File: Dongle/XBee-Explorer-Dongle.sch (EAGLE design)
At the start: 26 parts, among them U1 FT232RL-BASICSSOP, U2 XBEE-1B3, U3 V_REG_LDOSMD

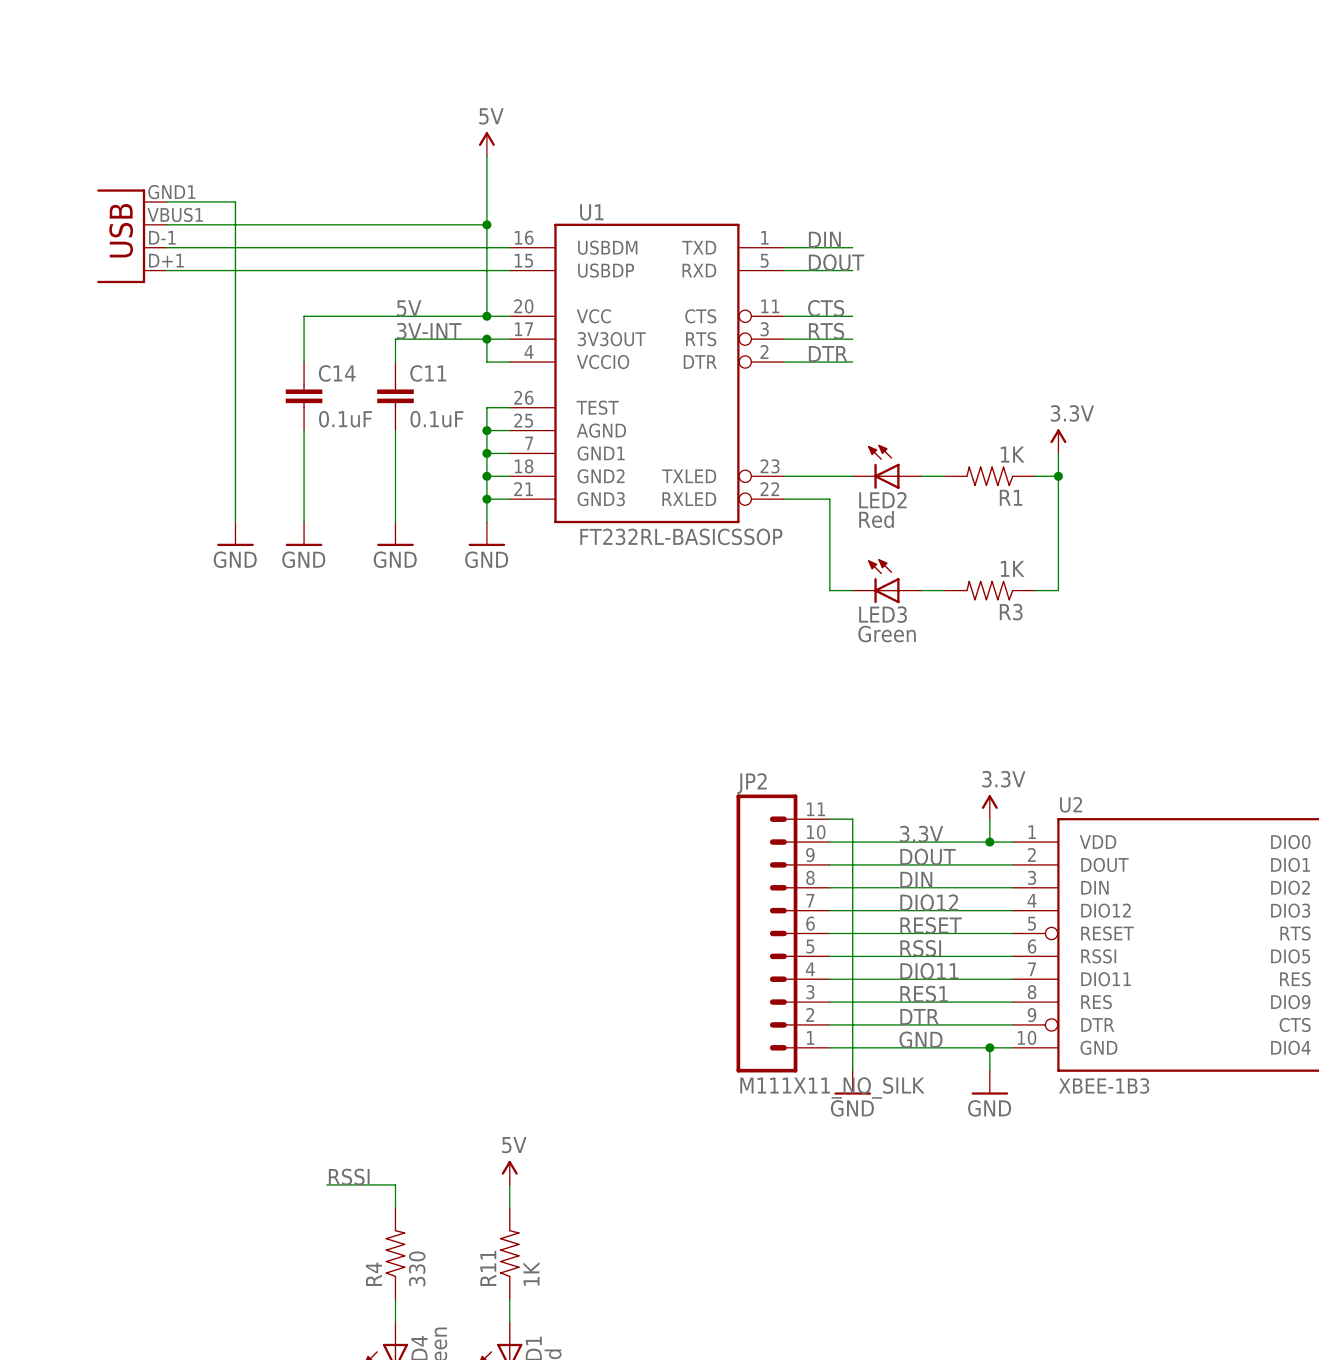
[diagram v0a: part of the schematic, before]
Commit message: XBee Dongle transition to FT231X
FT231X replaces the FT232RL.
Additional components added (R2, R5, C3, C4).
Updated all resistor and capacitor packages to 0603 footprints.
Rearranged Vreg circuit layout.
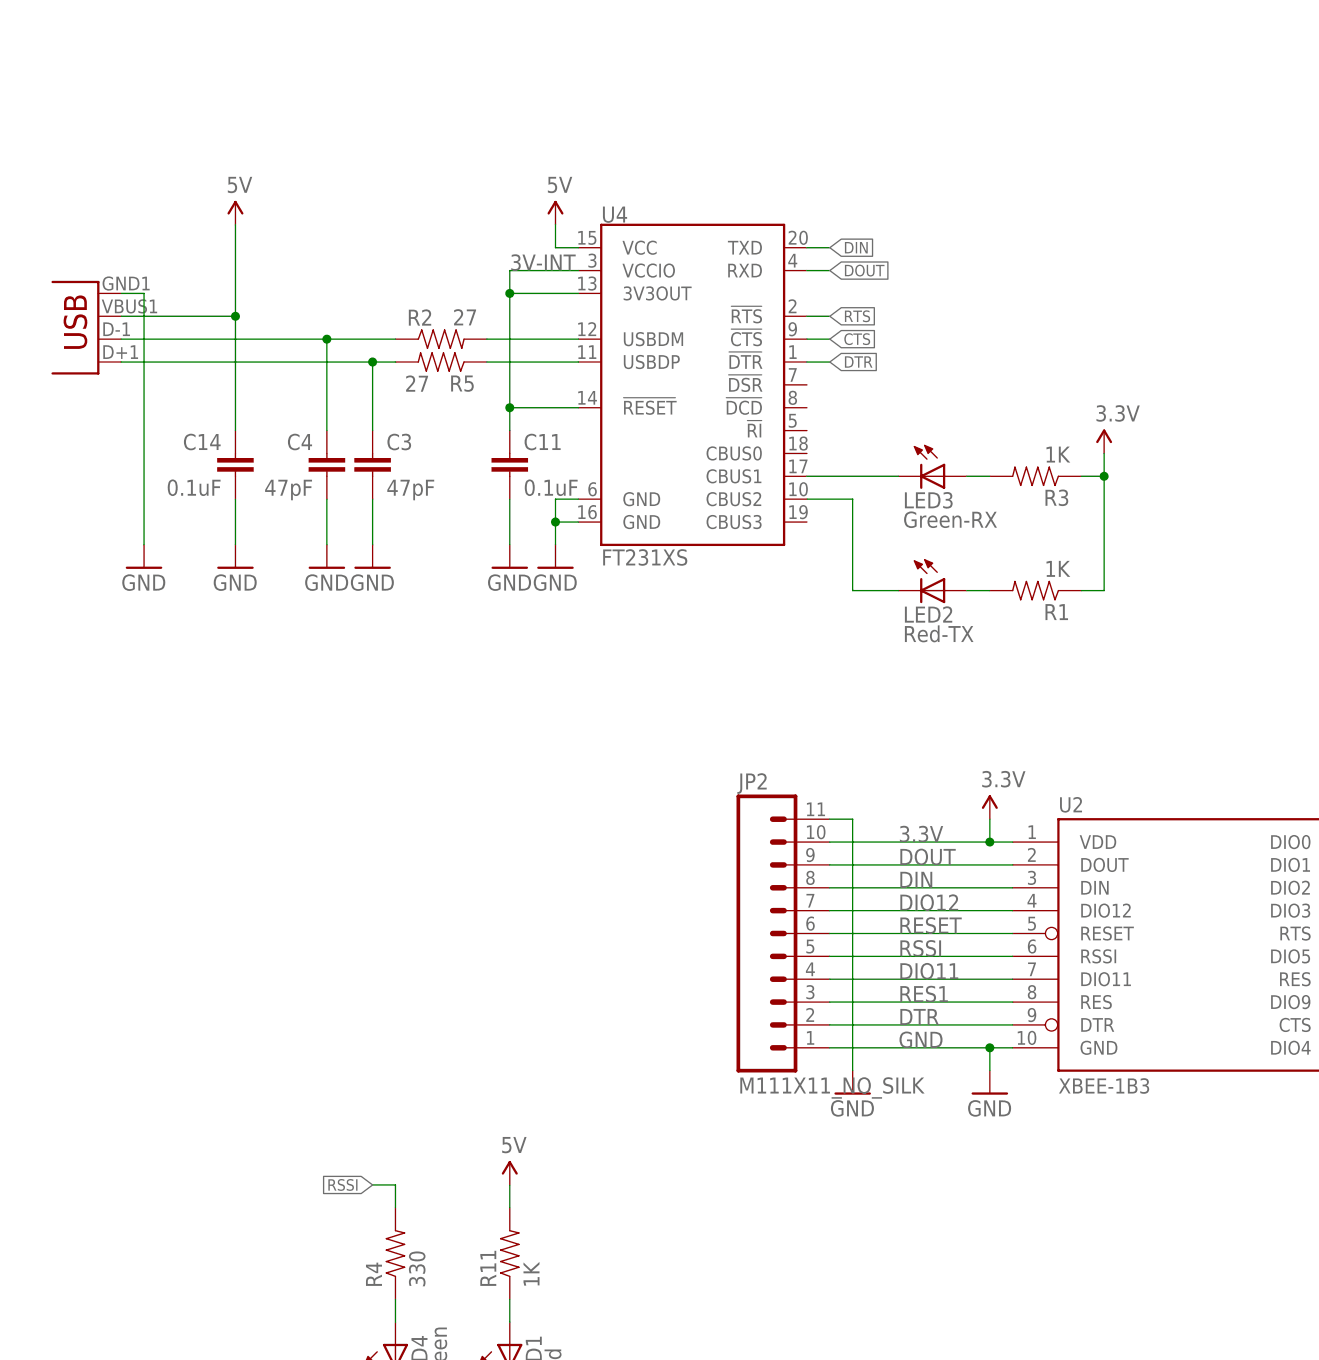
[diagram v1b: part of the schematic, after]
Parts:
- removed U1: FT232RL-BASICSSOP, SparkFun:FT232RL-BASICSSOP
- added C3, C4: 47pF, SparkFun:CAP0603-CAP
- added R2, R5: 27, SparkFun:RESISTOR0603-RES
- added U4: FT231XS, SparkFun-DigitalIC:FT231XS
- C11, C14, C2: device SparkFun:CAP0402-CAP -> SparkFun:CAP0603-CAP
- LED2: value Red -> Red-TX
- LED3: value Green -> Green-RX
- R1, R11, R3, R4: device SparkFun:RESISTOR0402-RES -> SparkFun:RESISTOR0603-RES
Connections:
- new net N$5: R2.2, U4.USBDM
- new net N$6: C3.1, JP1.D+, R5.2
- net 3V-INT: now also U4.!RESET, U4.3V3OUT, U4.VCCIO; no longer U1.3V3OUT, U1.VCCIO
- net 5V: now also U4.VCC; no longer U1.VCC
- net CTS: now also U4.!CTS; no longer U1.CTS
- net DIN: now also U4.TXD; no longer U1.TXD
- net DOUT: now also U4.RXD; no longer U1.RXD
- net DTR: now also U4.!DTR; no longer U1.DTR
- net GND: now also C3.2, C4.2, U4.GND@16, U4.GND@6; no longer U1.AGND, U1.GND1, U1.GND2, U1.GND3, U1.TEST
- net N$3: now also C4.1, R2.1; no longer U1.USBDM
- net N$7: now also R5.1, U4.USBDP; no longer JP1.D+, U1.USBDP
- net RTS: now also U4.!RTS; no longer U1.RTS
- net RXLED: now also U4.CBUS1; no longer U1.RXLED
- net TXLED: now also U4.CBUS2; no longer U1.TXLED
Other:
- moved on the sheet: C11, C14, LED2, LED3, R1, R3

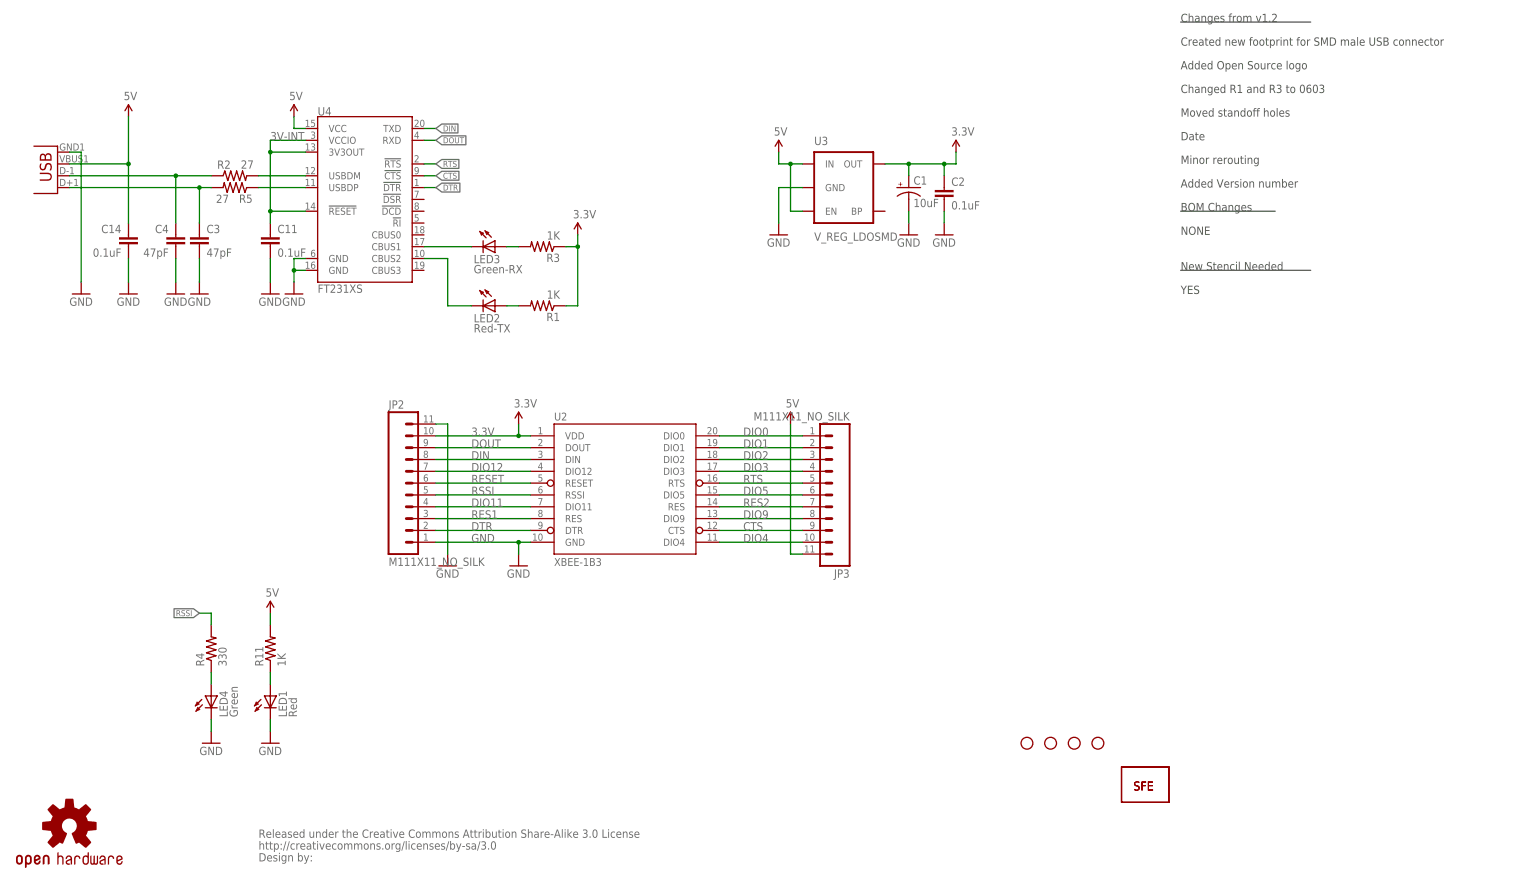
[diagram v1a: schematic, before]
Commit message: Added jumper to disconnect RSSI LED, moved silk
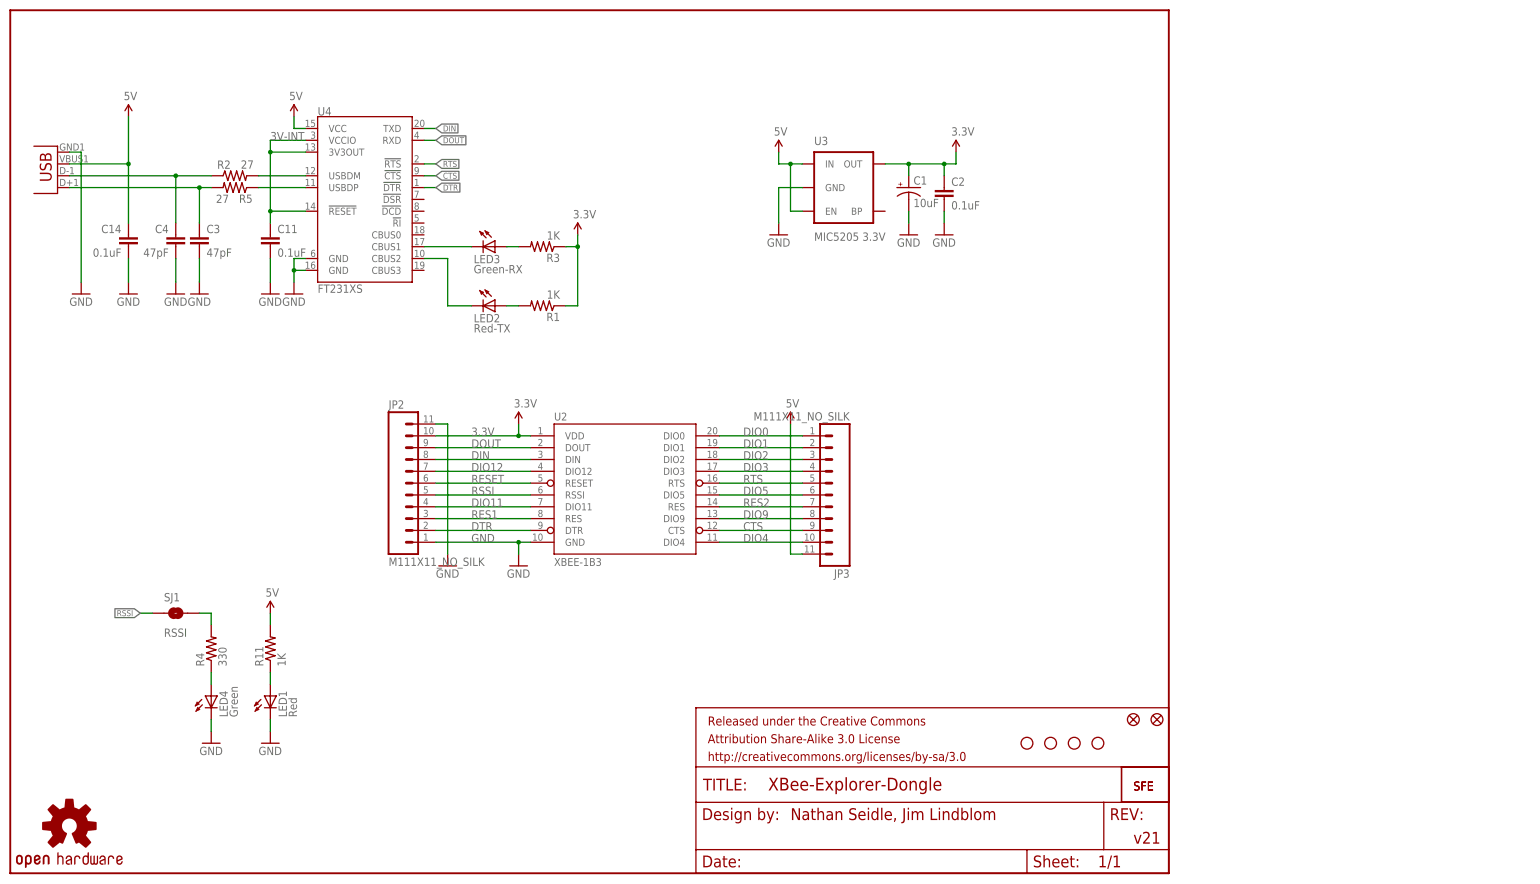
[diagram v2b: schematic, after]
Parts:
- removed U$8: OSHW-LOGOS, SparkFun:OSHW-LOGOS
- added FID1, FID2: FIDUCIALUFIDUCIAL, SparkFun-Aesthetics:FIDUCIALUFIDUCIAL
- added FRAME1: FRAME-LETTER, SparkFun-Aesthetics:FRAME-LETTER
- added SJ1: RSSI, SparkFun-Passives:SOLDERJUMPERTRACE
- U$7: value CREATIVE_COMMONS -> OSHW-LOGOS; device SparkFun:CREATIVE_COMMONS -> SparkFun:OSHW-LOGOS
- U3: value V_REG_LDOSMD -> MIC5205 3.3V
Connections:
- new net N$8: R4.2, SJ1.2
- net RSSI: now also SJ1.1; no longer R4.2
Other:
- note added: "Nathan Seidle, Jim Lindblom"
- note added: "v21"
- note removed: "Added Open Source logo"
- note removed: "Added Version number"
- note removed: "BOM Changes"
- note removed: "Changed R1 and R3 to 0603"
- note removed: "Changes from v1.2"
- note removed: "Created new footprint for SMD male USB connector"
- note removed: "Date"
- note removed: "Minor rerouting"
- note removed: "Moved standoff holes"
- note removed: "NONE"
- note removed: "New Stencil Needed"
- note removed: "YES"
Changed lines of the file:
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@@
 <?xml version="1.0" encoding="utf-8"?>
 <!DOCTYPE eagle SYSTEM "eagle.dtd">
-<eagle version="6.4">
+<eagle version="6.5.0">
 <drawing>
 <settings>
@@
 <layer number="106" name="bPlate" color="7" fill="1" visible="yes" active="yes"/>
 <layer number="107" name="Crop" color="7" fill="1" visible="yes" active="yes"/>
+<layer number="108" name="tplace-old" color="10" fill="1" visible="yes" active="yes"/>
+<layer number="109" name="ref-old" color="11" fill="1" visible="yes" active="yes"/>
 <layer number="116" name="Patch_BOT" color="9" fill="4" visible="yes" active="yes"/>
 <layer number="121" name="_tsilk" color="7" fill="1" visible="yes" active="yes"/>
@@
 </classes>
 <parts>
-<part name="FRAME1" library="SparkFun" deviceset="FRAME-LETTER" device=""/>
 <part name="C11" library="SparkFun" deviceset="CAP" device="0603-CAP" value="0.1uF"/>
 <part name="GND20" library="SparkFun" deviceset="GND" device=""/>
@@
 <part name="GND4" library="SparkFun" deviceset="GND" device=""/>
 <part name="P+2" library="SparkFun" deviceset="3.3V" device=""/>
-<part name="U3" library="SparkFun" deviceset="V_REG_LDO" device="SMD"/>
+<part name="U3" library="SparkFun" deviceset="V_REG_LDO" device="SMD" value="MIC5205 3.3V"/>
 <part name="GND1" library="SparkFun" deviceset="GND" device=""/>
 <part name="C1" library="SparkFun" deviceset="CAP_POL" device="1206" value="10uF"/>
@@
 <part name="U$6" library="SparkFun" deviceset="5V" device=""/>
 <part name="GND7" library="SparkFun" deviceset="GND" device=""/>
-<part name="U$7" library="SparkFun" deviceset="CREATIVE_COMMONS" device=""/>
-<part name="U$8" library="SparkFun" deviceset="OSHW-LOGO" device="S"/>
+<part name="U$7" library="SparkFun" deviceset="OSHW-LOGO" device="S"/>
 <part name="JP1" library="SparkFun-Connectors" deviceset="USB" device="A-SMD-MALE"/>
 <part name="U4" library="SparkFun-DigitalIC" deviceset="FT231X" device="S"/>
@@
 <part name="GND8" library="SparkFun" deviceset="GND" device=""/>
 <part name="GND9" library="SparkFun" deviceset="GND" device=""/>
+<part name="SJ1" library="SparkFun-Passives" deviceset="SOLDERJUMPER" device="TRACE" value="RSSI"/>
+<part name="FRAME1" library="SparkFun-Aesthetics" deviceset="FRAME-LETTER" device=""/>
+<part name="FID1" library="SparkFun-Aesthetics" deviceset="FIDUCIAL" device="UFIDUCIAL" value="FIDUCIALUFIDUCIAL"/>
+<part name="FID2" library="SparkFun-Aesthetics" deviceset="FIDUCIAL" device="UFIDUCIAL" value="FIDUCIALUFIDUCIAL"/>
 </parts>
 <sheets>
 <sheet>
 <plain>
-<wire x1="251.46" y1="182.88" x2="279.4" y2="182.88" width="0.2032" layer="97"/>
-<wire x1="251.46" y1="142.24" x2="271.78" y2="142.24" width="0.2032" layer="97"/>
-<wire x1="251.46" y1="129.54" x2="279.4" y2="129.54" width="0.2032" layer="97"/>
-<text x="251.46" y="182.88" size="1.778" layer="97">Changes from v1.2</text>
-<text x="251.46" y="177.8" size="1.778" layer="97">Created new footprint for SMD male USB connector</text>
-<text x="251.46" y="157.48" size="1.778" layer="97">Date</text>
-<text x="251.46" y="142.24" size="1.778" layer="97">BOM Changes</text>
-<text x="251.46" y="137.16" size="1.778" layer="97">NONE</text>
-<text x="251.46" y="129.54" size="1.778" layer="97">New Stencil Needed</text>
-<text x="251.46" y="124.46" size="1.778" layer="97">YES</text>
-<text x="251.46" y="152.4" size="1.778" layer="97">Minor rerouting </text>
-<text x="251.46" y="172.72" size="1.778" layer="97">Added Open Source logo</text>
-<text x="251.46" y="167.64" size="1.778" layer="97">Changed R1 and R3 to 0603</text>
-<text x="251.46" y="162.56" size="1.778" layer="97">Moved standoff holes</text>
-<text x="251.46" y="147.32" size="1.778" layer="97">Added Version number</text>
+<text x="167.64" y="12.7" size="2.54" layer="94" align="center-left">Nathan Seidle, Jim Lindblom</text>
+<text x="241.3" y="7.62" size="2.54" layer="94" align="center-left">v21</text>
 </plain>
 <instances>
-<instance part="FRAME1" gate="G$1" x="0" y="0"/>
-<instance part="FRAME1" gate="G$2" x="147.32" y="0"/>
 <instance part="C11" gate="G$1" x="55.88" y="134.62"/>
 <instance part="GND20" gate="1" x="55.88" y="124.46"/>
@@
 <instance part="U$6" gate="G$1" x="167.64" y="96.52"/>
 <instance part="GND7" gate="1" x="15.24" y="124.46"/>
-<instance part="U$7" gate="G$1" x="53.34" y="2.54"/>
-<instance part="U$8" gate="G$1" x="12.7" y="10.16"/>
+<instance part="U$7" gate="G$1" x="12.7" y="10.16"/>
 <instance part="JP1" gate="G$1" x="10.16" y="154.94" rot="R180"/>
 <instance part="U4" gate="G$1" x="76.2" y="144.78"/>
@@
 <instance part="GND8" gate="1" x="35.56" y="124.46"/>
 <instance part="GND9" gate="1" x="40.64" y="124.46"/>
+<instance part="SJ1" gate="1" x="35.56" y="55.88" smashed="yes">
+<attribute name="NAME" x="33.02" y="58.42" size="1.778" layer="95"/>
+<attribute name="VALUE" x="33.02" y="50.8" size="1.778" layer="96"/>
+</instance>
+<instance part="FRAME1" gate="G$1" x="0" y="0"/>
+<instance part="FRAME1" gate="G$2" x="147.32" y="0"/>
+<instance part="FID1" gate="G$1" x="246.38" y="33.02"/>
+<instance part="FID2" gate="G$1" x="241.3" y="33.02"/>
 </instances>
 <busses>
@@
 </segment>
 <segment>
-<wire x1="43.18" y1="53.34" x2="43.18" y2="55.88" width="0.1524" layer="91"/>
-<wire x1="43.18" y1="55.88" x2="40.64" y2="55.88" width="0.1524" layer="91"/>
-<pinref part="R4" gate="G$1" pin="2"/>
-<label x="40.64" y="55.88" size="1.27" layer="95" rot="R180" xref="yes"/>
+<wire x1="30.48" y1="55.88" x2="27.94" y2="55.88" width="0.1524" layer="91"/>
+<label x="27.94" y="55.88" size="1.27" layer="95" rot="R180" xref="yes"/>
+<pinref part="SJ1" gate="1" pin="1"/>
 </segment>
 </net>
@@
 </segment>
 </net>
+<net name="N$8" class="0">
+<segment>
+<pinref part="R4" gate="G$1" pin="2"/>
+<wire x1="43.18" y1="53.34" x2="43.18" y2="55.88" width="0.1524" layer="91"/>
+<pinref part="SJ1" gate="1" pin="2"/>
+<wire x1="43.18" y1="55.88" x2="40.64" y2="55.88" width="0.1524" layer="91"/>
+</segment>
+</net>
